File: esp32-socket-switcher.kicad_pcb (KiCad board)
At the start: 4 copper layers, 49.8 x 34.5 mm, 43 parts, among them IC1 ADP2301AUJZ-R7, J1 USB4110GFA, J2 4DB-P108-06, K1 G5CA-1A DC5, Q1 SS8050-G, Q2 SS8050-G, Q3 CSD17575Q3T, U2 ESP32-WROOM-32E-H4, U5 CP2102N-A02-GQFN24R

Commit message: added fuse. I feel i have been deceived...
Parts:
- added F1: Fuse 1A/300V, esp32-socket-switcher:FUSE_3519, F.Cu at (72.8, 71.8)
- added L2: SRR1206-122KL 1.2mH, esp32-socket-switcher:IND_BOURNS_SRR1240, F.Cu at (39.4, 71.3)
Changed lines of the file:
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@@
   (net 70 "/AC_LIVE")
   (net 71 "/SWITCH_IN")
+  (net 72 "Net-(F1-Pad2)")
   (footprint "esp32-socket-switcher:C_0603_1608Metric" (layer "F.Cu")
     (at 103.23 43.07)
@@
     )
   )
+  (footprint "esp32-socket-switcher:FUSE_3519" (layer "F.Cu")
+    (at 72.76 71.785 -90)
+    (property "MPN Fuse" "2JS 1.25-R")
+    (property "MPN Holder" "3519 (Keystone)")
+    (property "Sheetfile" "esp32-socket-switcher.kicad_sch")
+    (property "Sheetname" "")
+    (property "ki_description" "Fuse")
+    (property "ki_keywords" "fuse")
+    (attr through_hole)
+    (fp_text reference "F1" (at 0.165 -10.5 90) (layer "F.SilkS")
+        (effects (font (size 1 1) (thickness 0.15)))
+    )
+    (fp_text value "Fuse 1A/300V" (at 2.55 3.66 90) (layer "F.Fab")
+        (effects (font (size 1 1) (thickness 0.15)))
+    )
+    (fp_line (start -2.845 -9.4) (end -2.845 -8.74)
+      (stroke (width 0.127) (type solid)) (layer "F.SilkS"))
+    (fp_line (start -2.845 -9.4) (end 2.645 -9.4)
+      (stroke (width 0.127) (type solid)) (layer "F.SilkS"))
+    (fp_line (start -2.845 -6.04) (end -2.845 -5.01)
+      (stroke (width 0.127) (type solid)) (layer "F.SilkS"))
+    (fp_line (start -2.845 -5.01) (end 2.645 -5.01)
+      (stroke (width 0.127) (type solid)) (layer "F.SilkS"))
+    (fp_line (start -2.79 6.27) (end -2.79 5.24)
+      (stroke (width 0.127) (type solid)) (layer "F.SilkS"))
+    (fp_line (start -2.79 9.63) (end -2.79 8.97)
+      (stroke (width 0.127) (type solid)) (layer "F.SilkS"))
+    (fp_line (start 2.645 -9.4) (end 2.645 -8.74)
+      (stroke (width 0.127) (type solid)) (layer "F.SilkS"))
+    (fp_line (start 2.645 -6.04) (end 2.645 -5.01)
+      (stroke (width 0.127) (type solid)) (layer "F.SilkS"))
+    (fp_line (start 2.7 5.24) (end -2.79 5.24)
+      (stroke (width 0.127) (type solid)) (layer "F.SilkS"))
+    (fp_line (start 2.7 6.27) (end 2.7 5.24)
+      (stroke (width 0.127) (type solid)) (layer "F.SilkS"))
+    (fp_line (start 2.7 9.63) (end -2.79 9.63)
+      (stroke (width 0.127) (type solid)) (layer "F.SilkS"))
+    (fp_line (start 2.7 9.63) (end 2.7 8.97)
+      (stroke (width 0.127) (type solid)) (layer "F.SilkS"))
+    (fp_line (start -2.845 -9.4) (end 2.645 -9.4)
+      (stroke (width 0.127) (type solid)) (layer "F.Fab"))
+    (fp_line (start -2.845 -5.01) (end -2.845 -9.4)
+      (stroke (width 0.127) (type solid)) (layer "F.Fab"))
+    (fp_line (start -2.845 5.21) (end 2.645 5.21)
+      (stroke (width 0.127) (type solid)) (layer "F.Fab"))
+    (fp_line (start -2.845 9.6) (end -2.845 5.21)
+      (stroke (width 0.127) (type solid)) (layer "F.Fab"))
+    (fp_line (start 2.645 -9.4) (end 2.645 -5.01)
+      (stroke (width 0.127) (type solid)) (layer "F.Fab"))
+    (fp_line (start 2.645 -5.01) (end -2.845 -5.01)
+      (stroke (width 0.127) (type solid)) (layer "F.Fab"))
+    (fp_line (start 2.645 5.21) (end 2.645 9.6)
+      (stroke (width 0.127) (type solid)) (layer "F.Fab"))
+    (fp_line (start 2.645 9.6) (end -2.845 9.6)
+      (stroke (width 0.127) (type solid)) (layer "F.Fab"))
+    (pad "1" thru_hole circle (at -2.54 -6.5 270) (size 1.935 1.935) (drill 1.29) (layers "*.Cu" "*.Mask")
+      (net 70 "/AC_LIVE") (pintype "passive") (solder_mask_margin 0.102))
+    (pad "1" thru_hole circle (at 2.54 -6.5 270) (size 1.935 1.935) (drill 1.29) (layers "*.Cu" "*.Mask")
+      (net 70 "/AC_LIVE") (pintype "passive") (solder_mask_margin 0.102))
+    (pad "2" thru_hole circle (at -2.54 6.5 90) (size 1.935 1.935) (drill 1.29) (layers "*.Cu" "*.Mask")
+      (net 72 "Net-(F1-Pad2)") (pintype "passive") (solder_mask_margin 0.102))
+    (pad "2" thru_hole circle (at 2.54 6.5 180) (size 1.935 1.935) (drill 1.29) (layers "*.Cu" "*.Mask")
+      (net 72 "Net-(F1-Pad2)") (pintype "passive") (solder_mask_margin 0.102))
+    (model "${KIPRJMOD}/3dModels/3519.step"
+      (offset (xyz 0 4.75 0))
+      (scale (xyz 1 1 1))
+      (rotate (xyz -90 0 0))
+    )
+    (model "${KIPRJMOD}/3dModels/3519.step"
+      (offset (xyz 0 -4.75 0))
+      (scale (xyz 1 1 1))
+      (rotate (xyz -90 0 180))
+    )
+    (model "${KIPRJMOD}/3dModels/5x15 Fuse.STEP"
+      (offset (xyz 0 0 6.5))
+      (scale (xyz 1 1 1))
+      (rotate (xyz 0 0 90))
+    )
+  )
   (footprint "esp32-socket-switcher:R_0402_1005Metric" (layer "F.Cu")
     (at 91.19 42.75 -90)
@@
     )
   )
+  (footprint "esp32-socket-switcher:IND_BOURNS_SRR1240" (layer "F.Cu")
+    (at 39.445 71.325 90)
+    (tags "SRR1206-122KL ")
+    (property "Sheetfile" "esp32-socket-switcher.kicad_sch")
+    (property "Sheetname" "")
+    (property "ki_description" "Inductor")
+    (property "ki_keywords" "inductor choke coil reactor magnetic")
+    (attr smd)
+    (fp_text reference "L2" (at 0 0 90 unlocked) (layer "F.SilkS")
+        (effects (font (size 1 1) (thickness 0.15)))
+    )
+    (fp_text value "SRR1206-122KL 1.2mH" (at 0 0 90 unlocked) (layer "F.Fab")
+        (effects (font (size 1 1) (thickness 0.15)))
+    )
+    (fp_text user "${REFERENCE}" (at 0 0 90 unlocked) (layer "F.Fab")
+        (effects (font (size 1 1) (thickness 0.15)))
+    )
+    (fp_line (start -6.5278 -6.5278) (end -6.5278 -2.946881)
+      (stroke (width 0.1524) (type solid)) (layer "F.SilkS"))
+    (fp_line (start -6.5278 2.946881) (end -6.5278 6.5278)
+      (stroke (width 0.1524) (type solid)) (layer "F.SilkS"))
+    (fp_line (start -6.5278 6.5278) (end 6.5278 6.5278)
+      (stroke (width 0.1524) (type solid)) (layer "F.SilkS"))
+    (fp_line (start 6.5278 -6.5278) (end -6.5278 -6.5278)
+      (stroke (width 0.1524) (type solid)) (layer "F.SilkS"))
+    (fp_line (start 6.5278 -2.946881) (end 6.5278 -6.5278)
+      (stroke (width 0.1524) (type solid)) (layer "F.SilkS"))
+    (fp_line (start 6.5278 6.5278) (end 6.5278 2.946881)
+      (stroke (width 0.1524) (type solid)) (layer "F.SilkS"))
+    (fp_line (start -6.6548 -6.6548) (end 6.6548 -6.6548)
+      (stroke (width 0.1524) (type solid)) (layer "F.CrtYd"))
+    (fp_line (start -6.6548 -2.9591) (end -6.6548 -6.6548)
+      (stroke (width 0.1524) (type solid)) (layer "F.CrtYd"))
+    (fp_line (start -6.6548 -2.9591) (end -6.6548 -2.9591)
+      (stroke (width 0.1524) (type solid)) (layer "F.CrtYd"))
+    (fp_line (start -6.6548 2.9591) (end -6.6548 -2.9591)
+      (stroke (width 0.1524) (type solid)) (layer "F.CrtYd"))
+    (fp_line (start -6.6548 2.9591) (end -6.6548 2.9591)
+      (stroke (width 0.1524) (type solid)) (layer "F.CrtYd"))
+    (fp_line (start -6.6548 6.6548) (end -6.6548 2.9591)
+      (stroke (width 0.1524) (type solid)) (layer "F.CrtYd"))
+    (fp_line (start 6.6548 -6.6548) (end 6.6548 -2.9591)
+      (stroke (width 0.1524) (type solid)) (layer "F.CrtYd"))
+    (fp_line (start 6.6548 -2.9591) (end 6.6548 -2.9591)
+      (stroke (width 0.1524) (type solid)) (layer "F.CrtYd"))
+    (fp_line (start 6.6548 -2.9591) (end 6.6548 2.9591)
+      (stroke (width 0.1524) (type solid)) (layer "F.CrtYd"))
+    (fp_line (start 6.6548 2.9591) (end 6.6548 2.9591)
+      (stroke (width 0.1524) (type solid)) (layer "F.CrtYd"))
+    (fp_line (start 6.6548 2.9591) (end 6.6548 6.6548)
+      (stroke (width 0.1524) (type solid)) (layer "F.CrtYd"))
+    (fp_line (start 6.6548 6.6548) (end -6.6548 6.6548)
+      (stroke (width 0.1524) (type solid)) (layer "F.CrtYd"))
+    (fp_line (start -6.4008 -6.4008) (end -6.4008 6.4008)
+      (stroke (width 0.0254) (type solid)) (layer "F.Fab"))
+    (fp_line (start -6.4008 6.4008) (end 6.4008 6.4008)
+      (stroke (width 0.0254) (type solid)) (layer "F.Fab"))
+    (fp_line (start 6.4008 -6.4008) (end -6.4008 -6.4008)
+      (stroke (width 0.0254) (type solid)) (layer "F.Fab"))
+    (fp_line (start 6.4008 6.4008) (end 6.4008 -6.4008)
+      (stroke (width 0.0254) (type solid)) (layer "F.Fab"))
+    (fp_circle (center -6.3246 0) (end -6.3246 0)
+      (stroke (width 0.0254) (type solid)) (fill none) (layer "F.Fab"))
+    (pad "1" smd rect (at -4.8514 0 90) (size 2.8956 5.4102) (layers "F.Cu" "F.Paste" "F.Mask")
+      (net 72 "Net-(F1-Pad2)") (pinfunction "1") (pintype "passive"))
+    (pad "2" smd rect (at 4.8514 0 90) (size 2.8956 5.4102) (layers "F.Cu" "F.Paste" "F.Mask")
+      (net 65 "Net-(PS1-AC(L))") (pinfunction "2") (pintype "passive"))
+    (zone (net 0) (net_name "") (layer "F.Cu") (hatch full 0.508)
+      (connect_pads (clearance 0))
+      (min_thickness 0.254) (filled_areas_thickness no)
+      (keepout (tracks not_allowed) (vias not_allowed) (pads allowed) (copperpour not_allowed) (footprints allowed))
+      (fill (thermal_gap 0.508) (thermal_bridge_width 0.508))
+      (polygon
+        (pts
+          (xy 33.095 74.6778)
+          (xy 33.095 67.9722)
+          (xy 45.795 67.9722)
+          (xy 45.795 74.6778)
+        )
+      )
+    )
+    (model "${KIPRJMOD}/3dModels/IND_BOURNS_SRR1240.step"
+      (offset (xyz 0 0 0))
+      (scale (xyz 1 1 1))
+      (rotate (xyz 0 0 0))
+    )
+  )

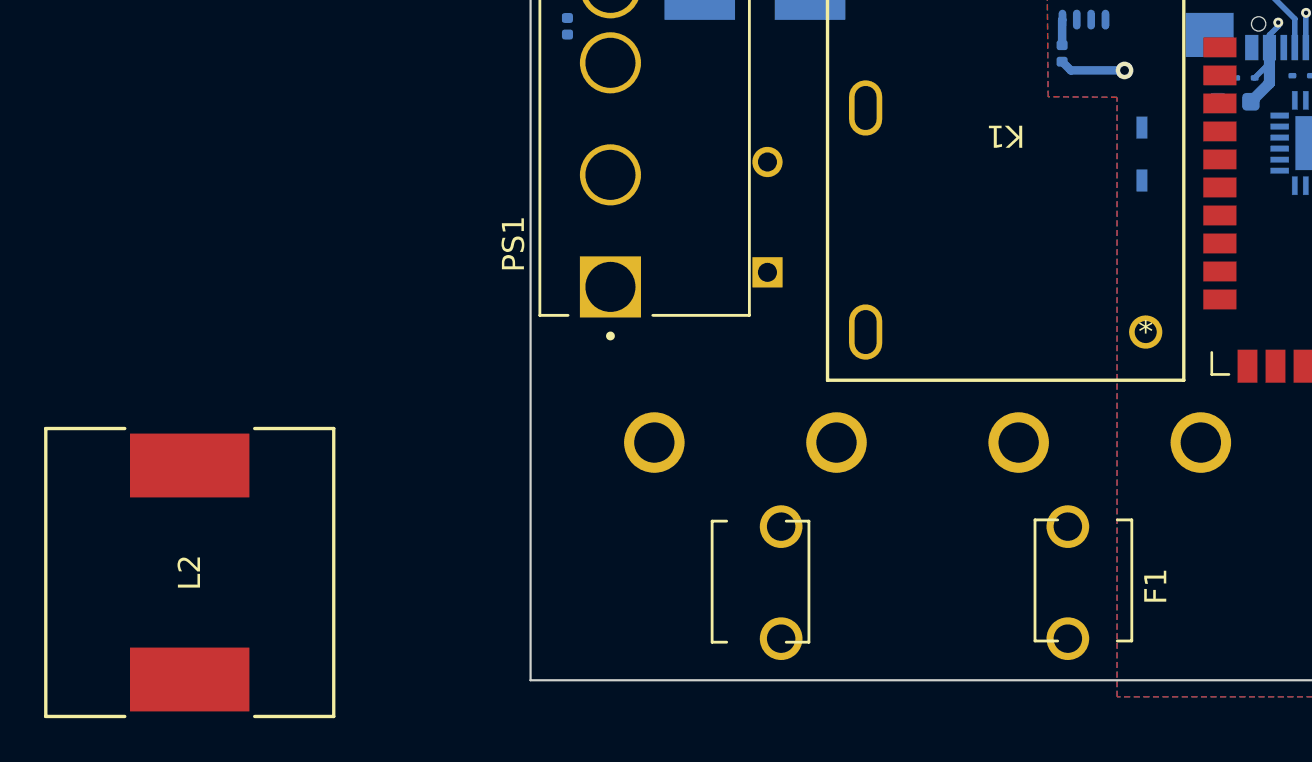
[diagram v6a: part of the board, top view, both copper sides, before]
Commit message: changed inductors, sticking with og converter
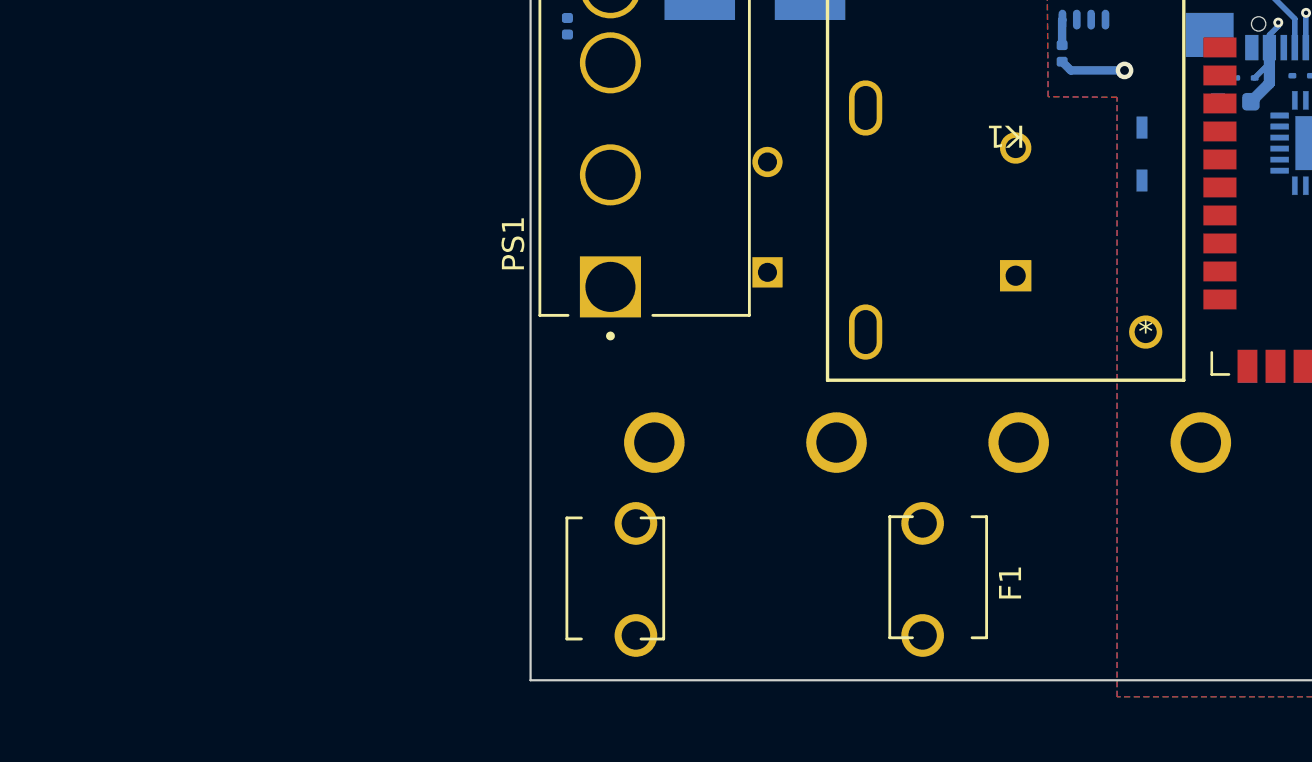
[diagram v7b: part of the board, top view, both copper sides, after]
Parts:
- L2: value SRR1206-122KL 1.2mH -> RLB1014-122KL; footprint esp32-socket-switcher:IND_BOURNS_SRR1240 -> esp32-socket-switcher:IND_BOURNS_RLB1014; moved to B.Cu
- moved L2 39.8 mm to (76.9, 57.9)
- moved F1 6.59 mm to (66.2, 71.6)
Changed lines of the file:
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@@
   )
   (footprint "esp32-socket-switcher:FUSE_3519" (layer "F.Cu")
-    (at 72.76 71.785 -90)
+    (at 66.175 71.64 -90)
     (property "MPN Fuse" "2JS 1.25-R")
     (property "MPN Holder" "3519 (Keystone)")
@@
       (scale (xyz 1 1 1))
       (rotate (xyz -90 0 90))
-    )
-  )
-  (footprint "esp32-socket-switcher:IND_BOURNS_SRR1240" (layer "F.Cu")
-    (at 39.445 71.325 90)
-    (tags "SRR1206-122KL ")
-    (property "Sheetfile" "esp32-socket-switcher.kicad_sch")
-    (property "Sheetname" "")
-    (property "ki_description" "Inductor")
-    (property "ki_keywords" "inductor choke coil reactor magnetic")
-    (attr smd)
-    (fp_text reference "L2" (at 0 0 90 unlocked) (layer "F.SilkS")
-        (effects (font (size 1 1) (thickness 0.15)))
-    )
-    (fp_text value "SRR1206-122KL 1.2mH" (at 0 0 90 unlocked) (layer "F.Fab")
-        (effects (font (size 1 1) (thickness 0.15)))
-    )
-    (fp_text user "${REFERENCE}" (at 0 0 90 unlocked) (layer "F.Fab")
-        (effects (font (size 1 1) (thickness 0.15)))
-    )
-    (fp_line (start -6.5278 -6.5278) (end -6.5278 -2.946881)
-      (stroke (width 0.1524) (type solid)) (layer "F.SilkS"))
-    (fp_line (start -6.5278 2.946881) (end -6.5278 6.5278)
-      (stroke (width 0.1524) (type solid)) (layer "F.SilkS"))
-    (fp_line (start -6.5278 6.5278) (end 6.5278 6.5278)
-      (stroke (width 0.1524) (type solid)) (layer "F.SilkS"))
-    (fp_line (start 6.5278 -6.5278) (end -6.5278 -6.5278)
-      (stroke (width 0.1524) (type solid)) (layer "F.SilkS"))
-    (fp_line (start 6.5278 -2.946881) (end 6.5278 -6.5278)
-      (stroke (width 0.1524) (type solid)) (layer "F.SilkS"))
-    (fp_line (start 6.5278 6.5278) (end 6.5278 2.946881)
-      (stroke (width 0.1524) (type solid)) (layer "F.SilkS"))
-    (fp_line (start -6.6548 -6.6548) (end 6.6548 -6.6548)
-      (stroke (width 0.1524) (type solid)) (layer "F.CrtYd"))
-    (fp_line (start -6.6548 -2.9591) (end -6.6548 -6.6548)
-      (stroke (width 0.1524) (type solid)) (layer "F.CrtYd"))
-    (fp_line (start -6.6548 -2.9591) (end -6.6548 -2.9591)
-      (stroke (width 0.1524) (type solid)) (layer "F.CrtYd"))
-    (fp_line (start -6.6548 2.9591) (end -6.6548 -2.9591)
-      (stroke (width 0.1524) (type solid)) (layer "F.CrtYd"))
-    (fp_line (start -6.6548 2.9591) (end -6.6548 2.9591)
-      (stroke (width 0.1524) (type solid)) (layer "F.CrtYd"))
-    (fp_line (start -6.6548 6.6548) (end -6.6548 2.9591)
-      (stroke (width 0.1524) (type solid)) (layer "F.CrtYd"))
-    (fp_line (start 6.6548 -6.6548) (end 6.6548 -2.9591)
-      (stroke (width 0.1524) (type solid)) (layer "F.CrtYd"))
-    (fp_line (start 6.6548 -2.9591) (end 6.6548 -2.9591)
-      (stroke (width 0.1524) (type solid)) (layer "F.CrtYd"))
-    (fp_line (start 6.6548 -2.9591) (end 6.6548 2.9591)
-      (stroke (width 0.1524) (type solid)) (layer "F.CrtYd"))
-    (fp_line (start 6.6548 2.9591) (end 6.6548 2.9591)
-      (stroke (width 0.1524) (type solid)) (layer "F.CrtYd"))
-    (fp_line (start 6.6548 2.9591) (end 6.6548 6.6548)
-      (stroke (width 0.1524) (type solid)) (layer "F.CrtYd"))
-    (fp_line (start 6.6548 6.6548) (end -6.6548 6.6548)
-      (stroke (width 0.1524) (type solid)) (layer "F.CrtYd"))
-    (fp_line (start -6.4008 -6.4008) (end -6.4008 6.4008)
-      (stroke (width 0.0254) (type solid)) (layer "F.Fab"))
-    (fp_line (start -6.4008 6.4008) (end 6.4008 6.4008)
-      (stroke (width 0.0254) (type solid)) (layer "F.Fab"))
-    (fp_line (start 6.4008 -6.4008) (end -6.4008 -6.4008)
-      (stroke (width 0.0254) (type solid)) (layer "F.Fab"))
-    (fp_line (start 6.4008 6.4008) (end 6.4008 -6.4008)
-      (stroke (width 0.0254) (type solid)) (layer "F.Fab"))
-    (fp_circle (center -6.3246 0) (end -6.3246 0)
-      (stroke (width 0.0254) (type solid)) (fill none) (layer "F.Fab"))
-    (pad "1" smd rect (at -4.8514 0 90) (size 2.8956 5.4102) (layers "F.Cu" "F.Paste" "F.Mask")
-      (net 72 "Net-(F1-Pad2)") (pinfunction "1") (pintype "passive"))
-    (pad "2" smd rect (at 4.8514 0 90) (size 2.8956 5.4102) (layers "F.Cu" "F.Paste" "F.Mask")
-      (net 65 "Net-(PS1-AC(L))") (pinfunction "2") (pintype "passive"))
-    (zone (net 0) (net_name "") (layer "F.Cu") (hatch full 0.508)
-      (connect_pads (clearance 0))
-      (min_thickness 0.254) (filled_areas_thickness no)
-      (keepout (tracks not_allowed) (vias not_allowed) (pads allowed) (copperpour not_allowed) (footprints allowed))
-      (fill (thermal_gap 0.508) (thermal_bridge_width 0.508))
-      (polygon
-        (pts
-          (xy 33.095 74.6778)
-          (xy 33.095 67.9722)
-          (xy 45.795 67.9722)
-          (xy 45.795 74.6778)
-        )
-      )
-    )
-    (model "${KIPRJMOD}/3dModels/IND_BOURNS_SRR1240.step"
-      (offset (xyz 0 0 0))
-      (scale (xyz 1 1 1))
-      (rotate (xyz 0 0 0))
     )
   )
@@
       (offset (xyz 0 0 0))
       (scale (xyz 1 1 1))
+      (rotate (xyz 0 0 0))
+    )
+  )
+  (footprint "esp32-socket-switcher:IND_BOURNS_RLB1014" (layer "B.Cu")
+    (at 76.895 57.86885 90)
+    (tags "RLB1014-122KL ")
+    (property "Sheetfile" "esp32-socket-switcher.kicad_sch")
+    (property "Sheetname" "")
+    (property "ki_description" "Inductor")
+    (property "ki_keywords" "inductor choke coil reactor magnetic")
+    (attr through_hole)
+    (fp_text reference "L2" (at 2.8956 0 270 unlocked) (layer "B.SilkS")
+        (effects (font (size 1 1) (thickness 0.15)) (justify mirror))
+    )
+    (fp_text value "RLB1014-122KL" (at 2.8956 0 270 unlocked) (layer "B.Fab")
+        (effects (font (size 1 1) (thickness 0.15)) (justify mirror))
+    )
+    (fp_text user "${REFERENCE}" (at 2.8956 0 270 unlocked) (layer "B.Fab")
+        (effects (font (size 1 1) (thickness 0.15)) (justify mirror))
+    )
+    (fp_line (start -3.2385 0) (end -1.9685 0)
+      (stroke (width 0.1524) (type solid)) (layer "B.SilkS"))
+    (fp_line (start -2.6035 0.635) (end -2.6035 -0.635)
+      (stroke (width 0.1524) (type solid)) (layer "B.SilkS"))
+    (fp_circle (center 2.8956 0) (end 7.6327 0)
+      (stroke (width 0.1524) (type solid)) (fill none) (layer "B.SilkS"))
+    (fp_line (start -1.9685 -2.002864) (end -1.9685 2.002864)
+      (stroke (width 0.0254) (type solid)) (layer "B.CrtYd"))
+    (fp_line (start -1.9685 2.002864) (end 0.892736 4.8641)
+      (stroke (width 0.0254) (type solid)) (layer "B.CrtYd"))
+    (fp_line (start 0.892736 -4.8641) (end -1.9685 -2.002864)
+      (stroke (width 0.0254) (type solid)) (layer "B.CrtYd"))
+    (fp_line (start 0.892736 4.8641) (end 4.898464 4.8641)
+      (stroke (width 0.0254) (type solid)) (layer "B.CrtYd"))
+    (fp_line (start 4.898464 -4.8641) (end 0.892736 -4.8641)
+      (stroke (width 0.0254) (type solid)) (layer "B.CrtYd"))
+    (fp_line (start 4.898464 4.8641) (end 7.7597 2.002864)
+      (stroke (width 0.0254) (type solid)) (layer "B.CrtYd"))
+    (fp_line (start 7.7597 -2.002864) (end 4.898464 -4.8641)
+      (stroke (width 0.0254) (type solid)) (layer "B.CrtYd"))
+    (fp_line (start 7.7597 2.002864) (end 7.7597 -2.002864)
+      (stroke (width 0.0254) (type solid)) (layer "B.CrtYd"))
+    (fp_line (start -3.2385 0) (end -1.9685 0)
+      (stroke (width 0.0254) (type solid)) (layer "B.Fab"))
+    (fp_line (start -2.6035 0.635) (end -2.6035 -0.635)
+      (stroke (width 0.0254) (type solid)) (layer "B.Fab"))
+    (fp_circle (center 2.8956 0) (end 7.5057 0)
+      (stroke (width 0.0254) (type solid)) (fill none) (layer "B.Fab"))
+    (pad "1" thru_hole rect (at 0 0 90) (size 1.4224 1.4224) (drill 0.9144) (layers "*.Cu" "*.Mask")
+      (net 72 "Net-(F1-Pad2)") (pinfunction "1") (pintype "passive"))
+    (pad "2" thru_hole circle (at 5.7912 0 90) (size 1.4224 1.4224) (drill 0.9144) (layers "*.Cu" "*.Mask")
+      (net 65 "Net-(PS1-AC(L))") (pinfunction "2") (pintype "passive"))
+    (model "${KIPRJMOD}/3dModels/IND_BOURNS_RLB1014.step"
+      (offset (xyz 0 0 0))
+      (scale (xyz 1 1 1))

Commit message: routing
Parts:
- C12: value 220uF/16V -> EEE-FK1C221XP
- C13: value 10uF/400V: 165-264VAC -> UCY2G100MPD
- moved D3 4.23 mm to (94.1, 60.7), turned to 180 degrees
- moved D2 1.49 mm to (94.2, 62.2)
- moved C13 0.73 mm to (65.4, 57.0)
- moved C3 0.71 mm to (102.6, 47.3)
- moved L2 0.52 mm to (76.4, 57.9)
- moved C5 0.50 mm to (86.3, 50.0)
- moved R7 0.47 mm to (83.9, 45.4), turned to 90 degrees
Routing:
- net 3v3: track 5.15 -> 57.9 mm, vias 0 -> 9
- net /VDC-WALL: track 0.00 -> 49.5 mm
- net Net-(F1-Pad2): track 0.00 -> 33.0 mm
- net /SWITCH_IN: track 1.36 -> 32.6 mm
- net /ESP32/IO0: track 0.00 -> 21.6 mm, vias 0 -> 1
- net /ESP32/CP210x_TX: track 0.00 -> 20.8 mm, vias 0 -> 1
- net Net-(PS1-AC(L)): track 0.00 -> 20.7 mm
- net /ESP32/CP210x_RX: track 0.00 -> 19.8 mm, vias 0 -> 1
- net /AC_LIVE_SWITCHED: track 0.00 -> 19.3 mm
- net /ESP32/RTS: track 0.00 -> 16.8 mm, vias 0 -> 2
- net /ESP32/DTR: track 0.00 -> 16.2 mm, vias 0 -> 2
- net /AC_LIVE: track 0.00 -> 16.1 mm
- net /VUSB: track 13.6 -> 29.5 mm
- net Net-(D7-A): track 0.00 -> 13.2 mm, vias 0 -> 1
- net Net-(PS1-+V(CAP)): track 0.00 -> 8.39 mm
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- added copper zone on B.Cu, net 3v3
- added copper zone on In1.Cu, net GND
- added copper zone on In2.Cu, net GND
